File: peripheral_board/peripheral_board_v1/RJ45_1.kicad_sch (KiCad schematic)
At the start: 10 parts

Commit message: Update to the board
Changed the WIZNET configuration to match that of the Pico2 eval board.
Changed the some names and some layout of the page. Not too much besides copying, reading as to why it is they way they made it and then applying.
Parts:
- added RJ6: RB1-125BAG1A, easyeda2kicad:RJ45-TH_RB1-125BAG1A, symbol easyeda2kicad:RB1-125BAG1A
- renumbered C31 to C33, C32 to C34, C33 to C35, C34 to C36, R17 to R19, R18 to R20, R19 to R21, R20 to R22, R21 to R23
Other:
- note added: "Note for me to remember"

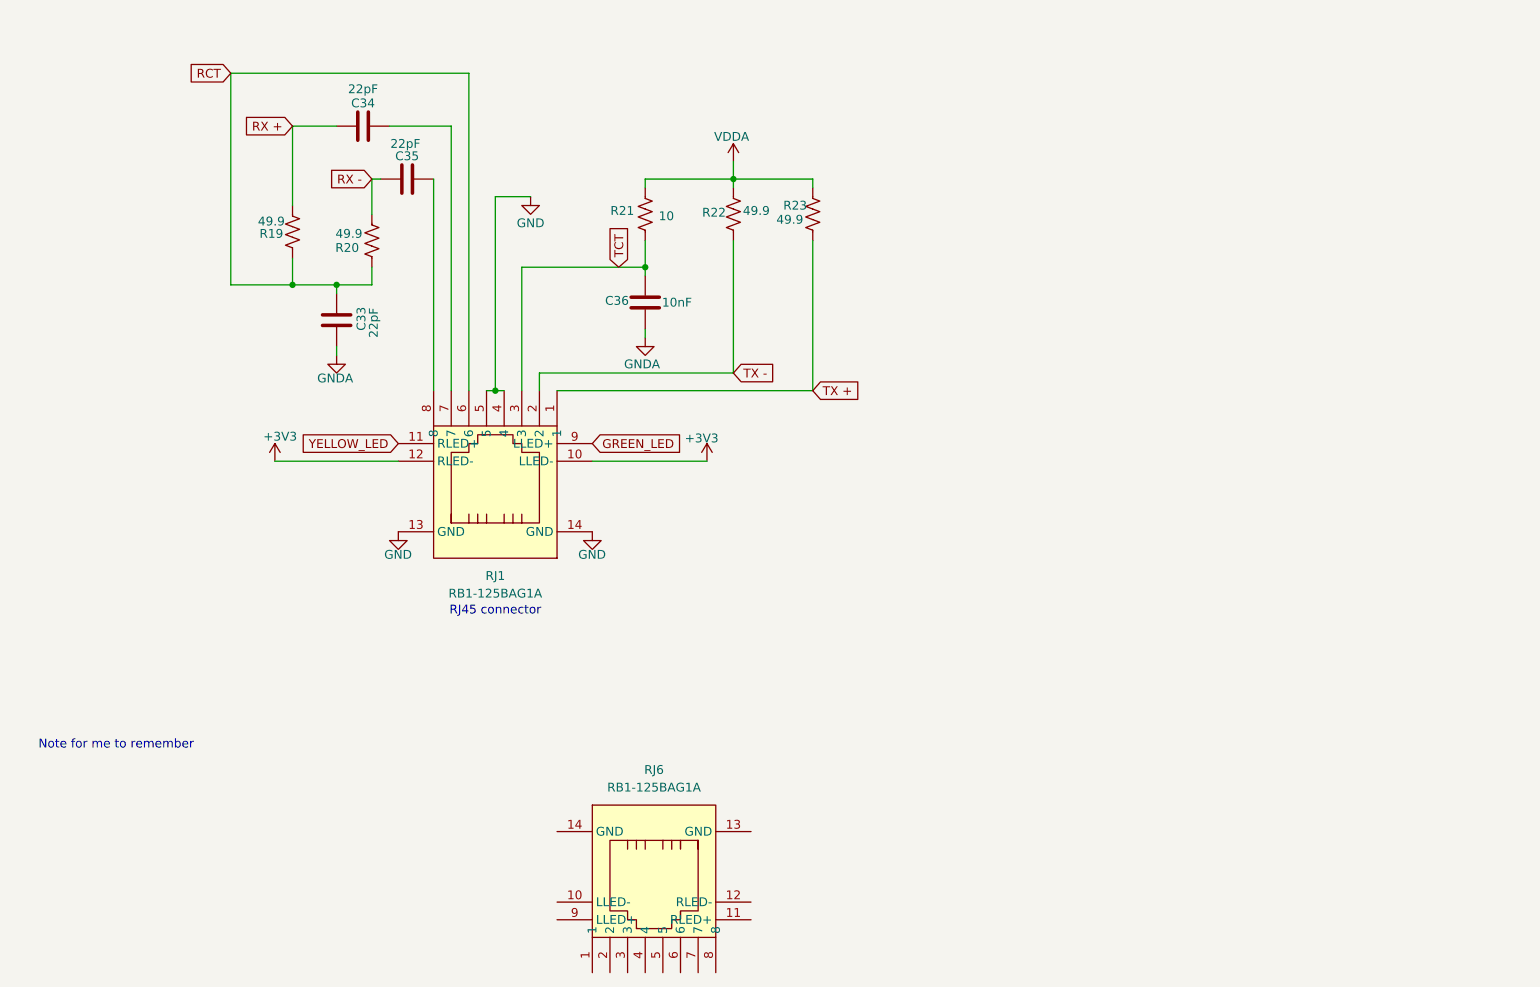
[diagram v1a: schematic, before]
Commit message: Update to the PCB
#Changes made so far

## Wiznet
* Changed the Wiznet layout to match that of their development board
* Restructured the RJ45 connections
    * *Looked over the RJ45 still a unsure*
    * Added in 2 differnt versions of Ethernt Connections. The one that shows the magnetics might be used for the Ethernet switch.
* Removed the Single Bus Buffer gate with 3-state output to match the dev board

## Raspberry Pi
* Moved to USB type C from micro USB for debugging.
* Changed the GPIO pins to match the Wiznet dev board.
* Brought in breakout pins for the rest of the GPIO.
* Cleaned up the Schematic to make it more clean.

## Ethernet Switch
* Changed the crystal to be the same as the Wiznet and to have the correct load caps
* Looking at the design check list to help get moving forward, need to relook at power distribution.
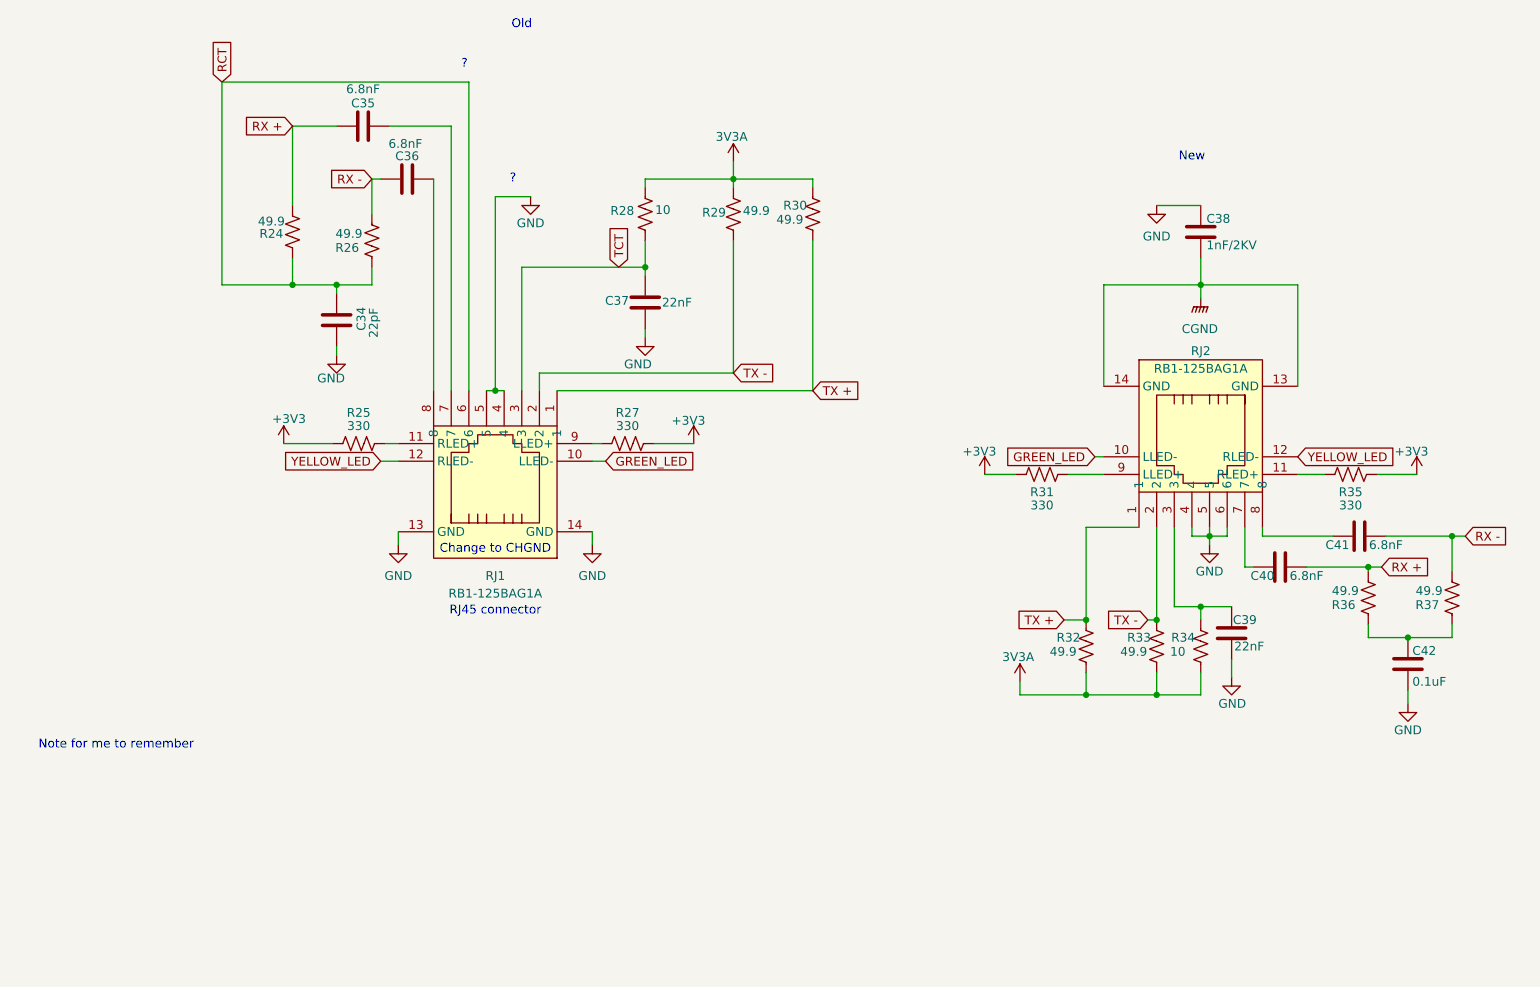
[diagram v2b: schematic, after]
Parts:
- removed RJ6: RB1-125BAG1A, easyeda2kicad:RJ45-TH_RB1-125BAG1A, symbol easyeda2kicad:RB1-125BAG1A
- added C38: 1nF/2KV, Capacitor_SMD:C_1808_4520Metric, symbol Device:C
- added C39: 22nF, Capacitor_SMD:C_0402_1005Metric, symbol Device:C
- added C40, C41: 6.8nF, Capacitor_SMD:C_0402_1005Metric, symbol Device:C
- added C42: 0.1uF, Capacitor_SMD:C_0402_1005Metric, symbol Device:C
- added R25, R27, R31, R35: 330, Resistor_SMD:R_0603_1608Metric, symbol Device:R_US
- added R32, R33, R36, R37: 49.9, Resistor_SMD:R_0603_1608Metric, symbol Device:R_US
- added R34: 10, Resistor_SMD:R_0603_1608Metric, symbol Device:R_US
- added RJ2: RB1-125BAG1A, easyeda2kicad:RJ45-TH_RB1-125BAG1A, symbol easyeda2kicad:RB1-125BAG1A
- C35: renamed from C34; value 22pF -> 6.8nF
- C36: renamed from C35; value 22pF -> 6.8nF
- C37: renamed from C36; value 10nF -> 22nF
- renumbered C33 to C34, R19 to R24, R20 to R26, R21 to R28, R22 to R29, R23 to R30
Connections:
- net GNDA is gone; now on net GND: C34.1, C37.1
- net +3V3: now also R25.2, R27.1, R31.2, R35.1; no longer RJ1.10 (LLED-), RJ1.12 (RLED-)
- net GND: now also C38.2, C39.2, C42.1, RJ2.4, RJ2.5, RJ2.6
- net GREEN_LED: now also RJ1.10 (LLED-), RJ2.10 (LLED-); no longer RJ1.9 (LLED+)
- net RX +: now also C40.1, R36.2
- net RX -: now also C41.1, R37.2
- net TX +: now also R32.2, RJ2.1
- net TX -: now also R33.2, RJ2.2
- net YELLOW_LED: now also RJ1.12 (RLED-), RJ2.12 (RLED-); no longer RJ1.11 (RLED+)
- net VDDA renamed 3V3A
- net 3V3A: now also R32.1, R33.1, R34.1
- new net: R27.2, RJ1.9 (LLED+)
- new net: C41.2, RJ2.8
- new net: R25.1, RJ1.11 (RLED+)
- new net: R35.2, RJ2.11 (RLED+)
- new net: C39.1, R34.2, RJ2.3
- new net: C40.2, RJ2.7
- new net: R31.1, RJ2.9 (LLED+)
- new net: C42.2, R36.1, R37.1
- new net CGND: C38.1, RJ2.13 (GND), RJ2.14 (GND)
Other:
- note added: "?"
- note added: "Change to CHGND"
- note added: "New"
- note added: "Old"

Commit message: Updated to the schematic
Kicad died on me so I needed to readd all my libraries to the project.

Added in the the Power board connector but want to go over it to make sure it will be implemented correctly. It is currently excluded.

Looked through the SALAD board and I had the same layout but I guess I did something wrong with selection of and or placement of signals traces. Added back in the single bus buffer, jumpers for changing the pmode and the filtering of the power and ground. It is currently excluded. Wiznet RJ45 connection is done.

Still going through the ethernet switch but found more info on the strap in mode. It is configured from the LED signals. The design guide has some specific details for the RJ45 and the Wiznet's RJ45 should be fine to use but I a Pulse JXD6-0001NL as a an easier stand in to better match the hardware design guideline. Still need to figure out the stand alone 4 port switch.
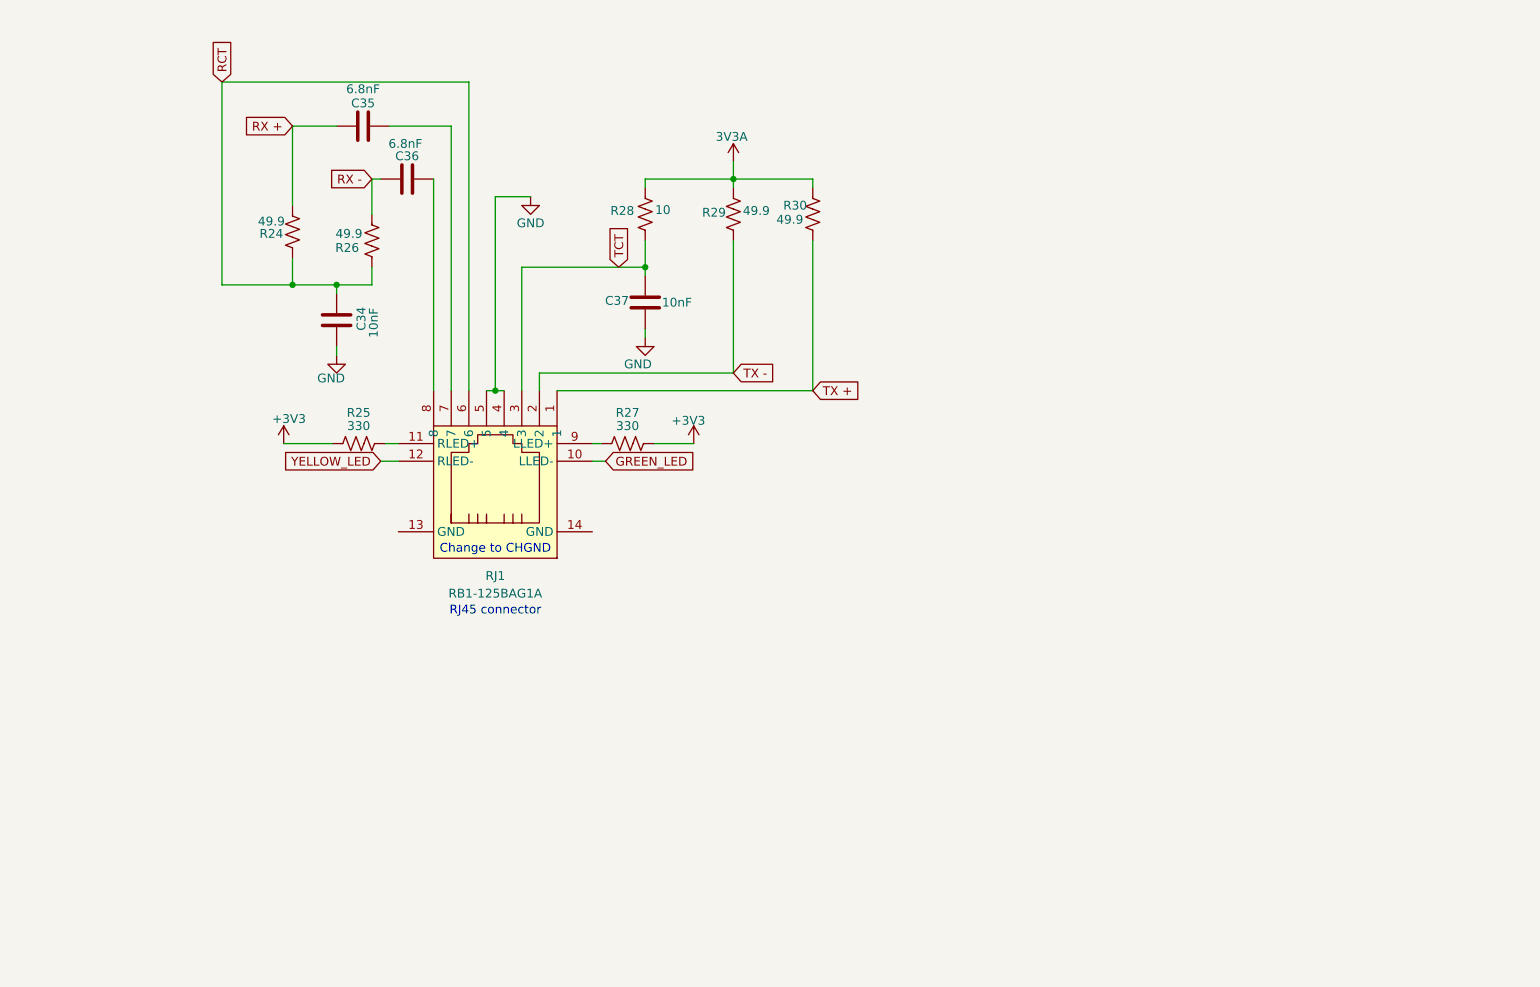
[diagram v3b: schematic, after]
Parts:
- removed C38: 1nF/2KV, Capacitor_SMD:C_1808_4520Metric, symbol Device:C
- removed C39: 22nF, Capacitor_SMD:C_0402_1005Metric, symbol Device:C
- removed C40, C41: 6.8nF, Capacitor_SMD:C_0402_1005Metric, symbol Device:C
- removed C42: 0.1uF, Capacitor_SMD:C_0402_1005Metric, symbol Device:C
- removed R31, R35: 330, Resistor_SMD:R_0603_1608Metric, symbol Device:R_US
- removed R32, R33, R36, R37: 49.9, Resistor_SMD:R_0603_1608Metric, symbol Device:R_US
- removed R34: 10, Resistor_SMD:R_0603_1608Metric, symbol Device:R_US
- removed RJ2: RB1-125BAG1A, easyeda2kicad:RJ45-TH_RB1-125BAG1A, symbol easyeda2kicad:RB1-125BAG1A
- C34: value 22pF -> 10nF
- C37: value 22nF -> 10nF
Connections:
- net GND: no longer RJ1.13 (GND), RJ1.14 (GND)
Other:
- note removed: "?"
- note removed: "New"
- note removed: "Note for me to remember"
- note removed: "Old"

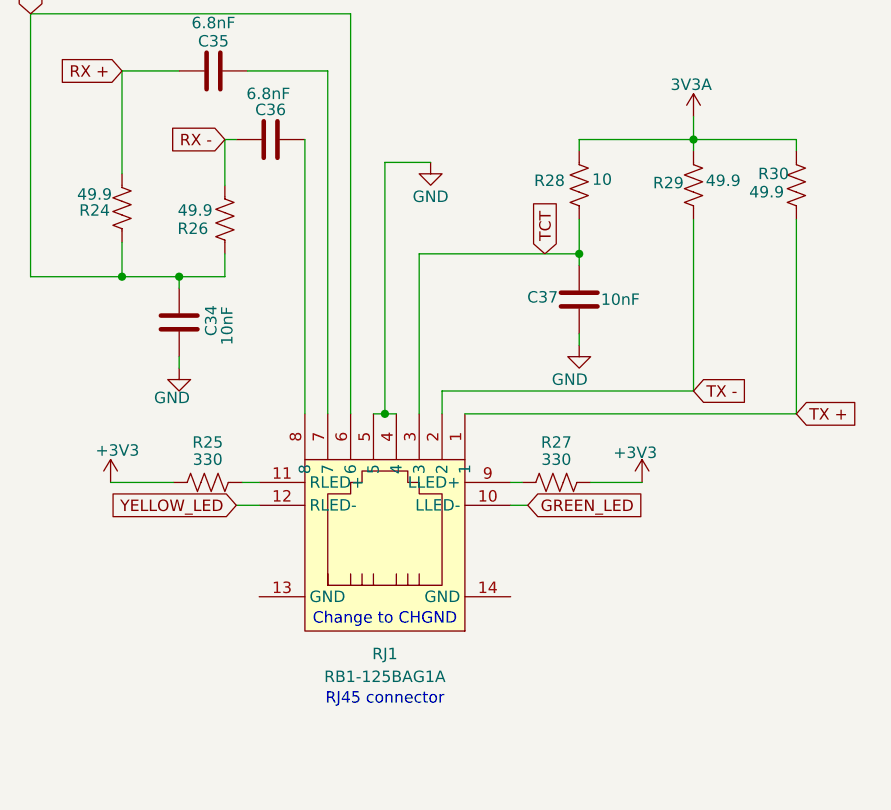
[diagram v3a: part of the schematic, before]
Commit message: Schematic design ready for review
Made the last changes for the Wiznet by adding in Dip switches and made sure that the interrupt and reset signals are attached to the raspberry pi.

Finished the Etherent switch by wiring the RJ45 port 1 with 2 configurations, leaning more towards not using the Wiznet port but might do it any ways for cost. Added test points to port 5 but might change it to be RMII configuration because the 4 port strap in mode sets it to that config. Put solder jumpers in for the LED strap in mode. On the schematic I put in a note about how to configure to the proper mode we want but after a review will change to be a hardwire set. Made the reset switch match that of the EVAL board but further reading found I do not need the diode. Created the VDDIO and VDDAT which are just 2 different versions of 3.3V. Layout would be next but need to learn more about trace integrity and impedance control.
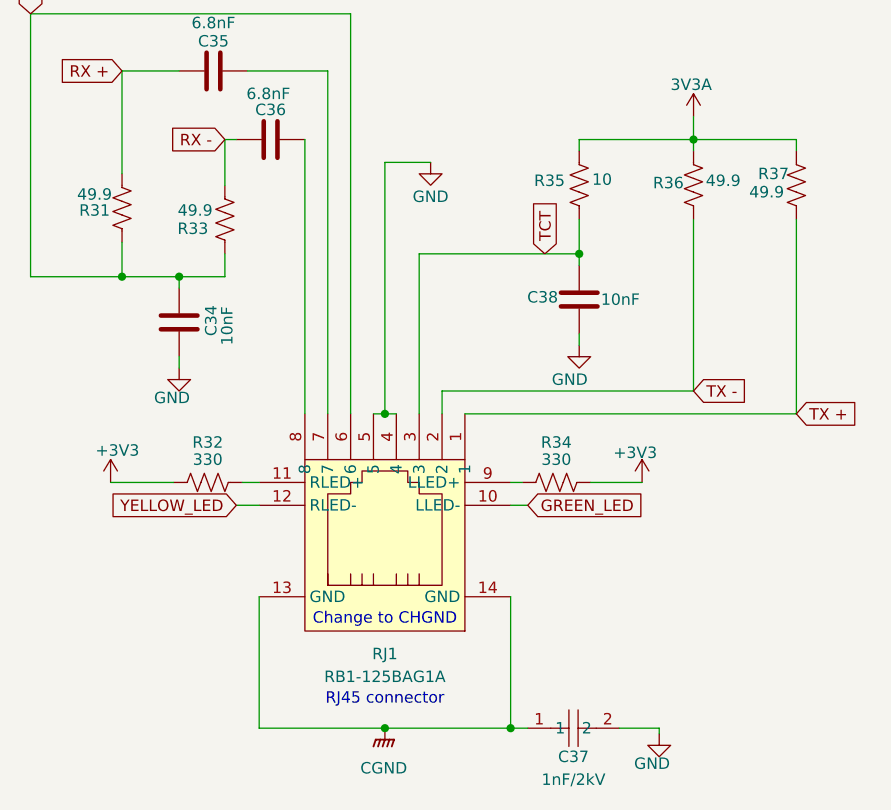
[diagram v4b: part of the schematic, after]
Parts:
- added C37: 1nF/2kV, SCALES:C1210, symbol SCALES:FV32N102J202EFG
- renumbered C37 to C38, R24 to R31, R25 to R32, R26 to R33, R27 to R34, R28 to R35, R29 to R36, R30 to R37
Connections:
- net GND: now also C37.2
- net CGND: now reaches RJ1.13 (GND)
- net CGND: now also RJ1.14 (GND), C37.1

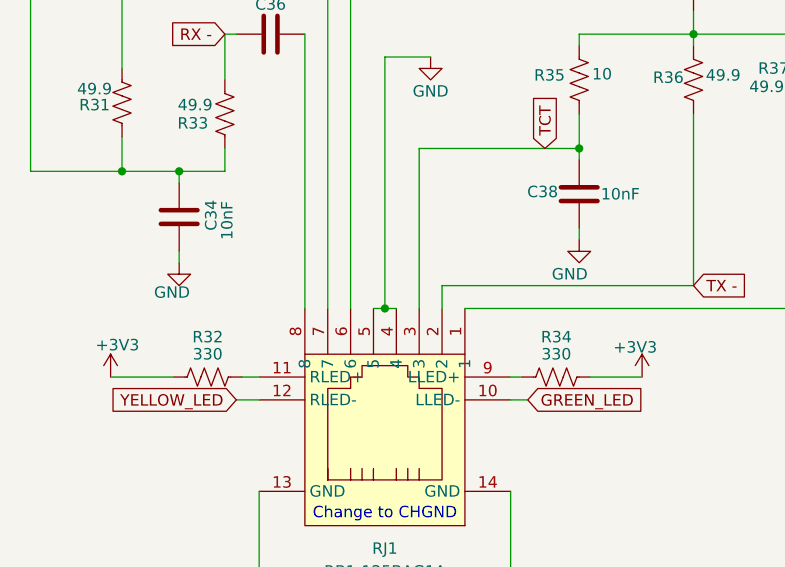
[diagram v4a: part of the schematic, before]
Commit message: Started the PCB layout
Finished the schematic. Now working on the PCB. Might looking in to moving to a 6 layer board.
Need to do a bit of redesign because changing some of the parts had different footprints.

Started on the Wiznet and the its RJ45 port it has. Want to make the port close to the chip as a possible. Currently working on the 4 layer stack up but if I switch to a 6 layer it might help with impedance and change the overall signal layering.
Almost done with the Wiznet just need to do the clock and the TX/RX pairs.
Once that is done I will work on the Ethernet switch then lastly the breakout pins for the RP.

I should have selected either a 6 layer or 4 layer board, leaning more towards 6 layer because I can keep my signals separated by the 3 and 3 sections.
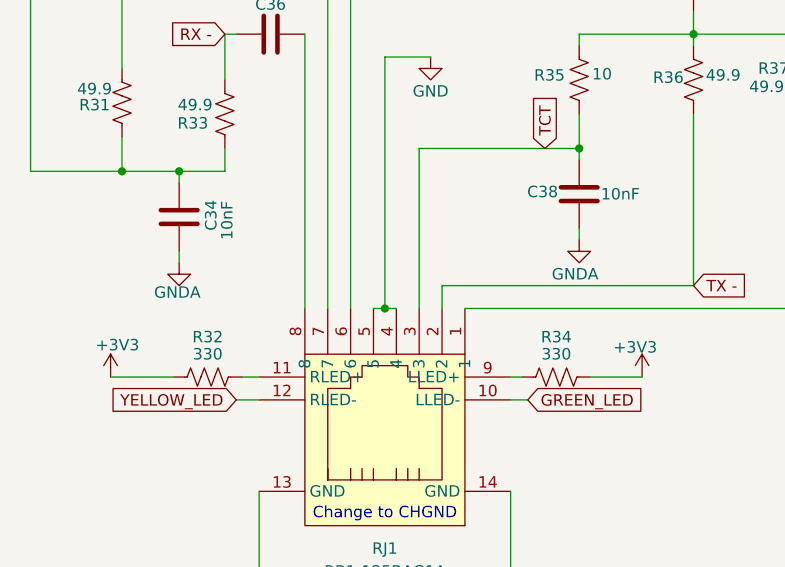
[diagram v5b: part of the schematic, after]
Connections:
- net GND: no longer C34.1, C38.1
- new net GNDA: C34.1, C38.1
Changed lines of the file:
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@@
 			)
 		)
-		(property "Value" "GND"
+		(property "Value" "GNDA"
 			(at 134.112 88.9 0)
 			(effects
@@
 			)
 		)
-		(property "Value" "GND"
+		(property "Value" "GNDA"
 			(at 89.916 90.932 0)
 			(effects
